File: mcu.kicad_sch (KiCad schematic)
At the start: 37 parts, among them J5 Conn_01x02, Q5 Q_NPN_BEC, Q6 Q_NPN_BEC, Q7 Q_NPN_BEC, Q8 Q_NPN_BEC, Q9 Q_NPN_BEC, U10 TJA1042T-3, U2 CH32V103C8T6, U3 XTSD01G, Y1 16MHz, Y2 32.768kHz

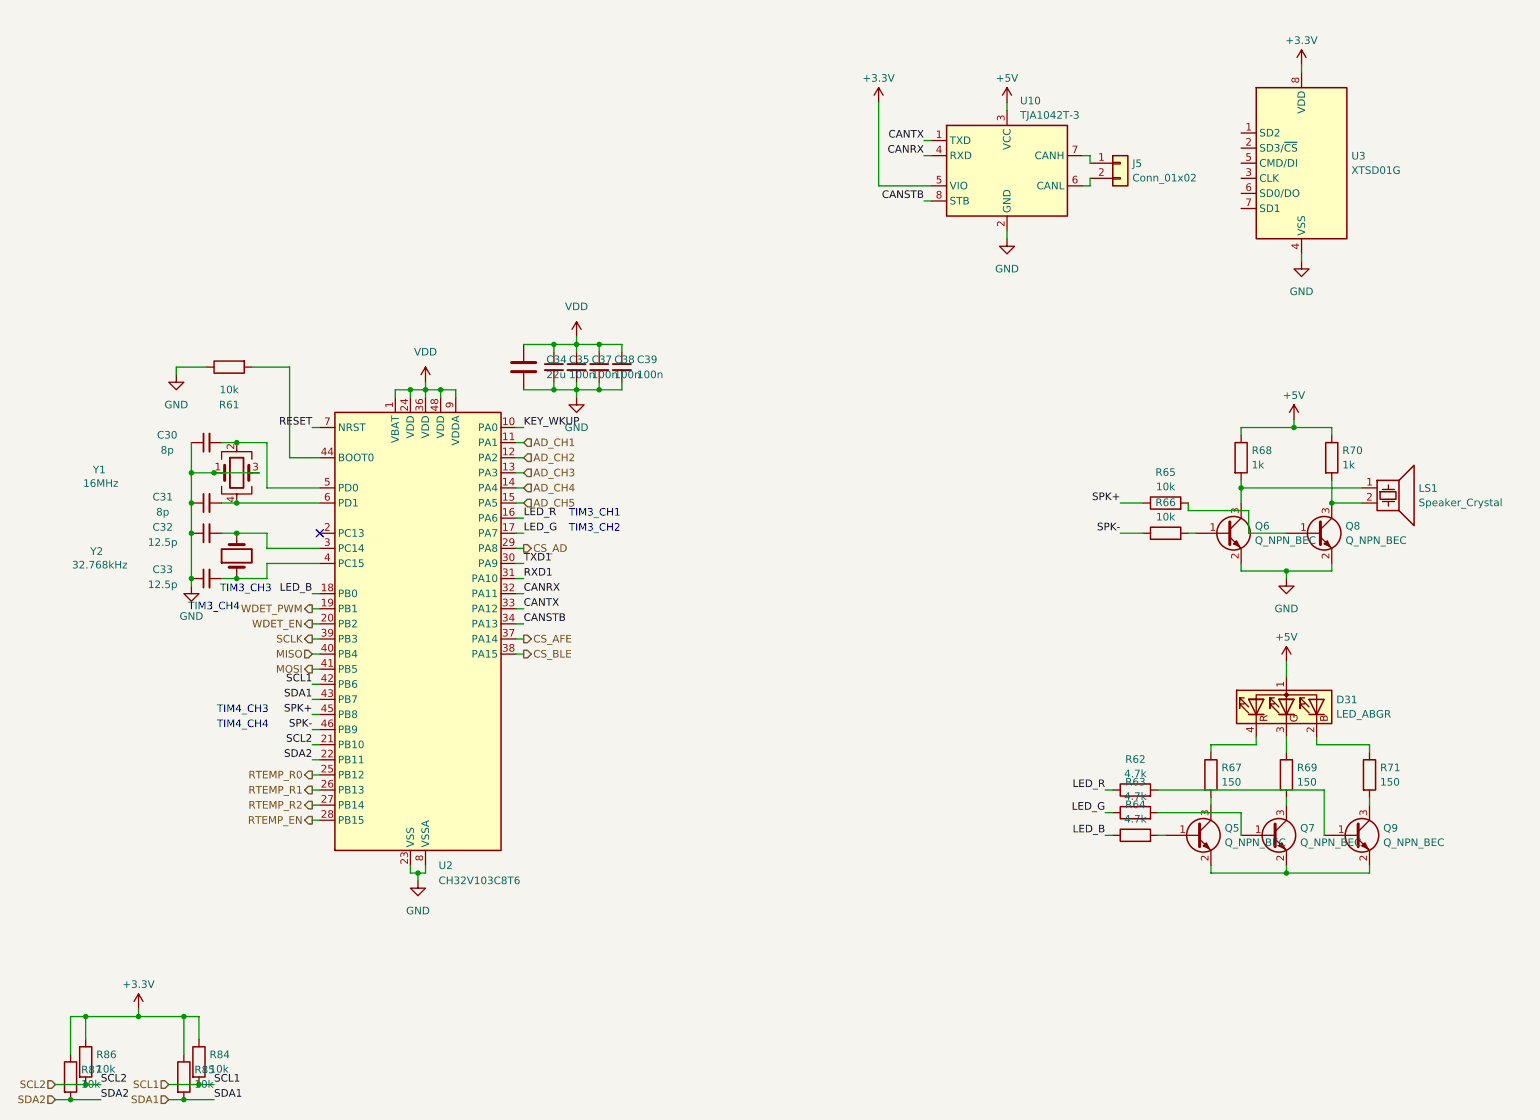
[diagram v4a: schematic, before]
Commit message: 分配封装，添加RS485通信接口，调整布局，传感器连接到独立MCU上
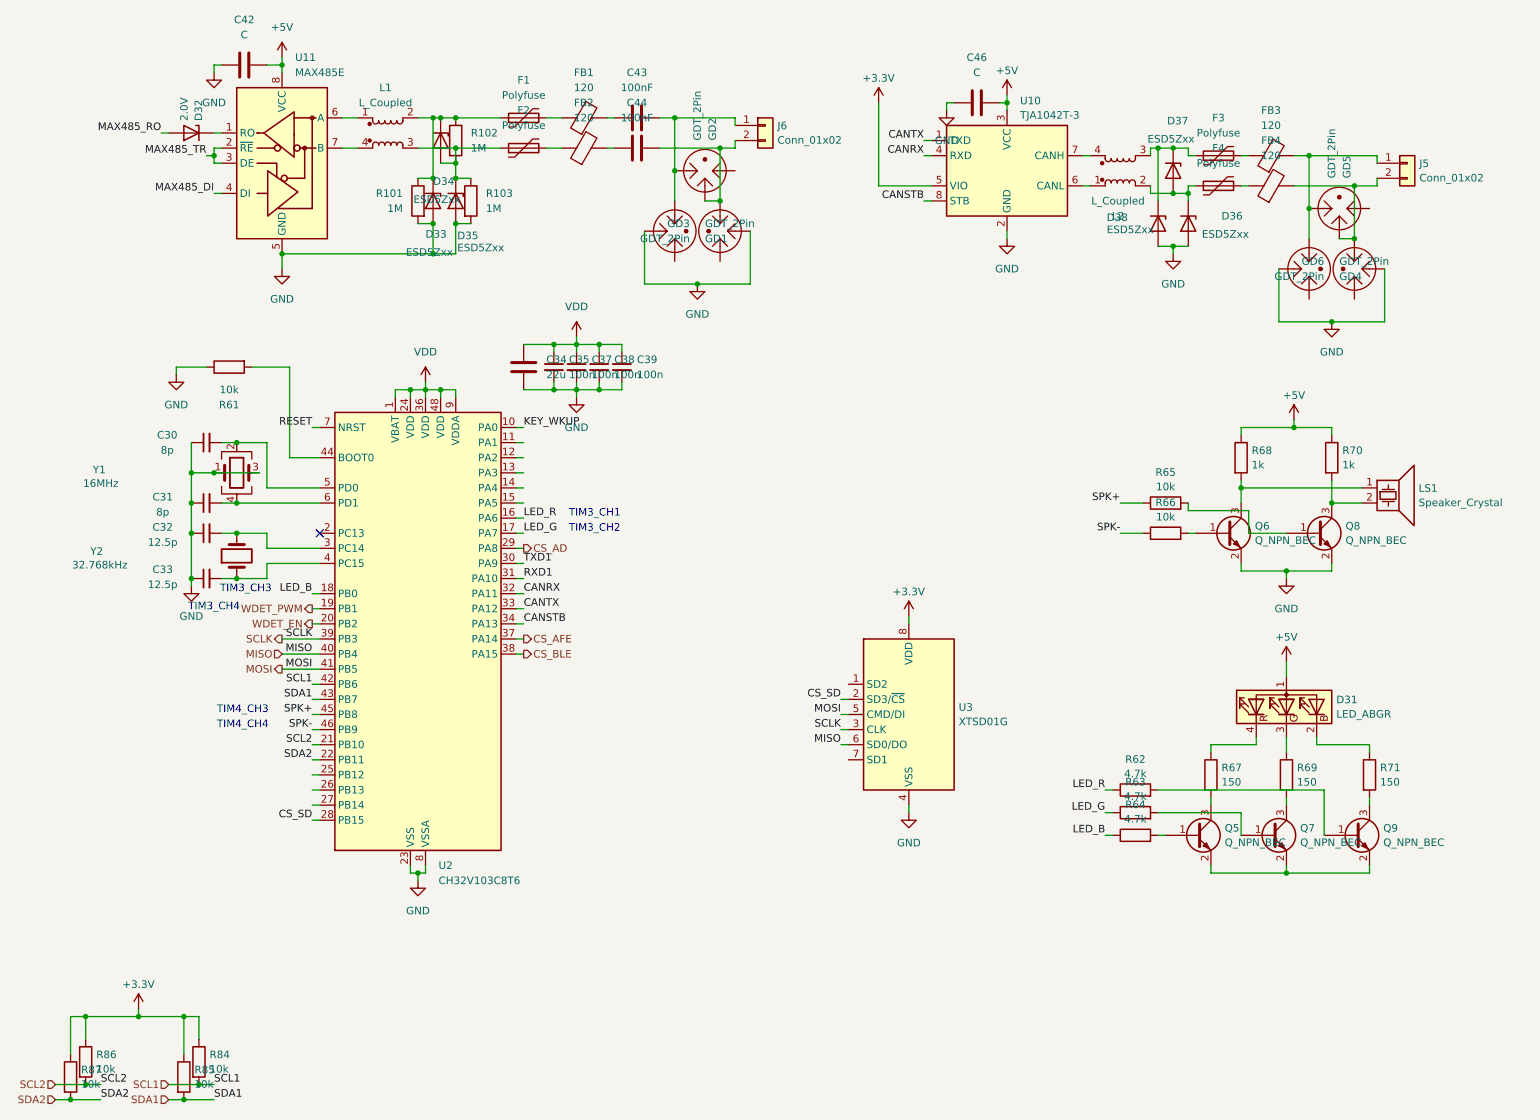
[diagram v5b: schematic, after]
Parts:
- added C42, C46: C, Capacitor_SMD:C_0603_1608Metric, symbol Device:C
- added C43, C44: 100nF, Capacitor_SMD:C_0603_1608Metric, symbol Device:C
- added D32: 2.0V, Diode_SMD:D_SOD-523, symbol Device:D_Zener
- added D33, D34, D35, D36, D37, D38: ESD5Zxx, Diode_SMD:D_SOD-523, symbol Diode:ESD5Zxx
- added F1, F2, F3, F4: Polyfuse, Fuse:Fuse_0603_1608Metric, symbol Device:Polyfuse
- added FB1, FB2, FB3, FB4: 120, Inductor_SMD:L_0603_1608Metric, symbol Device:FerriteBead
- added GD1, GD2, GD3, GD4, GD5, GD6: GDT_2Pin, Capacitor_SMD:C_1206_3216Metric, symbol Device:GDT_3Pin
- added J6: Conn_01x02, Connector_PinHeader_2.54mm:PinHeader_1x02_P2.54mm_Vertical, symbol Connector_Generic:Conn_01x02
- added L1, L2: L_Coupled, Inductor_SMD:L_CommonModeChoke_Coilcraft_1812CAN, symbol Device:L_Coupled_1243
- added R101, R102, R103: 1M, Resistor_SMD:R_0603_1608Metric, symbol Device:R
- added U11: MAX485E, Package_SO:SOIC-8_3.9x4.9mm_P1.27mm, symbol Interface_UART:MAX485E
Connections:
- net RTEMP_EN is gone; now on net CS_SD: U2.28 (PB15)
- net +5V: now also C42.2, C46.2, U11.8 (VCC)
- net GND: now also C42.1, C46.1, D33.2 (A), D35.2 (A), D36.2 (A), D38.2 (A), GD1.2, GD3.2, GD4.2, GD6.2, R101.2, R103.2, U11.5 (GND)
- net MISO: now also U3.6 (SD0/DO)
- net MOSI: now also U3.5 (CMD/DI)
- net SCLK: now also U3.3 (CLK)
- net CS_SD: now reaches U3.2 (SD3/~{CS})
- net at U10.6 (CANL): now also L2.1; no longer J5.2 (Pin_2)
- net at U10.7 (CANH): now also L2.4; no longer J5.1 (Pin_1)
- net AD_CH1: no longer names the net of U2.11 (PA1)
- net AD_CH2: no longer names the net of U2.12 (PA2)
- net AD_CH3: no longer names the net of U2.13 (PA3)
- net AD_CH4: no longer names the net of U2.14 (PA4)
- net AD_CH5: no longer names the net of U2.15 (PA5)
- net RTEMP_R0: no longer names the net of U2.25 (PB12)
- net RTEMP_R1: no longer names the net of U2.26 (PB13)
- net RTEMP_R2: no longer names the net of U2.27 (PB14)
- new net: C43.2, GD1.1, GD2.1, J6.1 (Pin_1)
- new net: C44.2, GD2.2, GD3.1, J6.2 (Pin_2)
- new net: D37.1 (K), D38.1 (K), F3.1, L2.3
- new net: F3.2, FB3.1
- new net: C44.1, FB2.2
- new net: FB3.2, GD4.1, GD5.1, J5.1 (Pin_1)
- new net: FB4.2, GD5.2, GD6.1, J5.2 (Pin_2)
- new net: F1.2, FB1.1
- new net: C43.1, FB1.2
- new net: D33.1 (K), D34.1 (K), F1.1, L1.2, R101.1, R102.1
- new net: D34.2 (A), D35.1 (K), F2.1, L1.3, R102.2, R103.1
- new net: F2.2, FB2.1
- new net: D36.1 (K), D37.2 (A), F4.1, L2.2
- new net: L1.1, U11.6 (A)
- new net: L1.4, U11.7 (B)
- new net: F4.2, FB4.1
- new net: D32.1 (K), U11.1 (RO)
- new net MAX485_DI: U11.4 (DI)
- new net MAX485_RO: D32.2 (A)
- new net MAX485_TR: U11.2 (~{RE}), U11.3 (DE)
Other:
- moved on the sheet: J5, U3

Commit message: 修改电源电路
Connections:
- net VDD is gone; now on net +3.3V: C34.1, C35.1, C37.1, C38.1, C39.1, U2.1 (VBAT), U2.24 (VDD), U2.36 (VDD), U2.48 (VDD), U2.9 (VDDA)
- net WDET_EN: no longer names the net of U2.20 (PB2)
- net WDET_PWM: no longer names the net of U2.19 (PB1)
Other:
- note added: "TODO: 添加一个电子墨水屏接口，用于显示电量等信息"
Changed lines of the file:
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@@
 		)
 	)
+	(text "TODO: 添加一个电子墨水屏接口，用于显示电量等信息"
+		(exclude_from_sim no)
+		(at 128.016 173.228 0)
+		(effects
+			(font
+				(size 1.27 1.27)
+			)
+		)
+	)
 	(text "TIM3_CH1"
 		(exclude_from_sim no)
@@
 		)
 	)
-	(hierarchical_label "WDET_PWM"
-		(shape output)
-		(at 64.77 111.76 180)
-		(effects
-			(font
-				(size 1.27 1.27)
-			)
-			(justify right)
-		)
-	)
 	(hierarchical_label "SDA2"
 		(shape input)
@@
 		)
 	)
-	(hierarchical_label "WDET_EN"
-		(shape output)
-		(at 64.77 114.3 180)
-		(effects
-			(font
-				(size 1.27 1.27)
-			)
-			(justify right)
-		)
-	)
 	(hierarchical_label "SCLK"
 		(shape output)
@@
 	)
 	(symbol
+		(lib_id "power:+3.3V")
+		(at 83.82 73.66 0)
+		(unit 1)
+		(exclude_from_sim no)
+		(in_bom yes)
+		(on_board yes)
+		(dnp no)
+		(fields_autoplaced yes)
+		(property "Reference" "#PWR58"
+			(at 83.82 77.47 0)
+			(effects
+				(font
+					(size 1.27 1.27)
+				)
+				(hide yes)
+			)
+		)
+		(property "Value" "+3.3V"
+			(at 83.82 69.5269 0)
+			(effects
+				(font
+					(size 1.27 1.27)
+				)
+			)
+		)
+		(property "Footprint" ""
+			(at 83.82 73.66 0)
+			(effects
+				(font
+					(size 1.27 1.27)
+				)
+				(hide yes)
+			)
+		)
+		(property "Datasheet" ""
+			(at 83.82 73.66 0)
+			(effects
+				(font
+					(size 1.27 1.27)
+				)
+				(hide yes)
+			)
+		)
+		(property "Description" "Power symbol creates a global label with name \"+3.3V\""
+			(at 83.82 73.66 0)
+			(effects
+				(font
+					(size 1.27 1.27)
+				)
+				(hide yes)
+			)
+		)
+		(pin "1"
+		)
+		(instances
+			(project "bmsboard_17s"
+				(path "/8b3bc3d6-55f6-430e-b34e-509c7be416f4/9405bd40-8890-47bd-a302-177d902533bf"
+					(reference "#PWR58")
+					(unit 1)
+				)
+			)
+		)
+	)
+	(symbol
 		(lib_id "power:+5V")
 		(at 228.6 120.65 0)
@@
 	)
 	(symbol
-		(lib_id "power:VDD")
-		(at 83.82 73.66 0)
-		(unit 1)
-		(exclude_from_sim no)
-		(in_bom yes)
-		(on_board yes)
-		(dnp no)
-		(fields_autoplaced yes)
-		(property "Reference" "#PWR17"
-			(at 83.82 77.47 0)
-			(effects
-				(font
-					(size 1.27 1.27)
-				)
-				(hide yes)
-			)
-		)
-		(property "Value" "VDD"
-			(at 83.82 68.58 0)
-			(effects
-				(font
-					(size 1.27 1.27)
-				)
-			)
-		)
-		(property "Footprint" ""
-			(at 83.82 73.66 0)
-			(effects
-				(font
-					(size 1.27 1.27)
-				)
-				(hide yes)
-			)
-		)
-		(property "Datasheet" ""
-			(at 83.82 73.66 0)
-			(effects
-				(font
-					(size 1.27 1.27)
-				)
-				(hide yes)
-			)
-		)
-		(property "Description" ""
-			(at 83.82 73.66 0)
-			(effects
-				(font
-					(size 1.27 1.27)
-				)
-				(hide yes)
-			)
-		)
-		(pin "1"
-		)
-		(instances
-			(project "bmsboard_17s"
-				(path "/8b3bc3d6-55f6-430e-b34e-509c7be416f4/9405bd40-8890-47bd-a302-177d902533bf"
-					(reference "#PWR17")
-					(unit 1)
-				)
-			)
-		)
-	)
-	(symbol
 		(lib_id "Device:Q_NPN_BEC")
 		(at 240.03 149.86 0)
@@
 	)
 	(symbol
+		(lib_id "power:+3.3V")
+		(at 109.22 66.04 0)
+		(unit 1)
+		(exclude_from_sim no)
+		(in_bom yes)
+		(on_board yes)
+		(dnp no)
+		(fields_autoplaced yes)
+		(property "Reference" "#PWR59"
+			(at 109.22 69.85 0)
+			(effects
+				(font
+					(size 1.27 1.27)
+				)
+				(hide yes)
+			)
+		)
+		(property "Value" "+3.3V"
+			(at 109.22 61.9069 0)
+			(effects
+				(font
+					(size 1.27 1.27)
+				)
+			)
+		)
+		(property "Footprint" ""
+			(at 109.22 66.04 0)
+			(effects
+				(font
+					(size 1.27 1.27)
+				)
+				(hide yes)
+			)
+		)
+		(property "Datasheet" ""
+			(at 109.22 66.04 0)
+			(effects
+				(font
+					(size 1.27 1.27)
+				)
+				(hide yes)
+			)
+		)
+		(property "Description" "Power symbol creates a global label with name \"+3.3V\""
+			(at 109.22 66.04 0)
+			(effects
+				(font
+					(size 1.27 1.27)
+				)
+				(hide yes)
+			)
+		)
+		(pin "1"
+		)
+		(instances
+			(project "bmsboard_17s"
+				(path "/8b3bc3d6-55f6-430e-b34e-509c7be416f4/9405bd40-8890-47bd-a302-177d902533bf"
+					(reference "#PWR59")
+					(unit 1)
+				)
+			)
+		)
+	)
+	(symbol
 		(lib_id "Device:Q_NPN_BEC")
 		(at 233.68 99.06 0)
@@
 					(unit 1)
 				)
-			)
-		)
-	)
-	(symbol
-		(lib_id "power:VDD")
-		(at 109.22 66.04 0)
-		(unit 1)
-		(exclude_from_sim no)
-		(in_bom yes)
-		(on_board yes)
-		(dnp no)
-		(fields_autoplaced yes)
-		(property "Reference" "#PWR18"
-			(at 109.22 69.85 0)
-			(effects
-				(font
-					(size 1.27 1.27)
-				)
-				(hide yes)
-			)
-		)
-		(property "Value" "VDD"
-			(at 109.22 60.96 0)
-			(effects
-				(font
-					(size 1.27 1.27)
-				)
-			)
-		)
-		(property "Footprint" ""
-			(at 109.22 66.04 0)
-			(effects
-				(font
-					(size 1.27 1.27)
-				)
-				(hide yes)
-			)
-		)
-		(property "Datasheet" ""
-			(at 109.22 66.04 0)
-			(effects
-				(font
-					(size 1.27 1.27)
-				)
-				(hide yes)
-			)
-		)
-		(property "Description" ""
-			(at 109.22 66.04 0)
-			(effects
-				(font
-					(size 1.27 1.27)
-				)
-				(hide yes)
-			)
-		)
-		(pin "1"
-		)
-		(instances
-			(project "bmsboard_17s"
-				(path "/8b3bc3d6-55f6-430e-b34e-509c7be416f4/9405bd40-8890-47bd-a302-177d902533bf"
-					(reference "#PWR18")
-					(unit 1)
-				)
